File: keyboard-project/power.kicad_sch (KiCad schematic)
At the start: 0 parts

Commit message: working on power
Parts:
- added J1: Conn_01x02, symbol Connector_Generic:Conn_01x02
- added U1: MCP1826S, symbol Regulator_Linear:MCP1826S
- added U2: MCP73871, Package_DFN_QFN:QFN-20-1EP_4x4mm_P0.5mm_EP2.5x2.5mm, symbol Battery_Management:MCP73871
- added U3: XC6206PxxxMR, Package_TO_SOT_SMD:SOT-23-3, symbol Regulator_Linear:XC6206PxxxMR
- added U4: AP7331-28WG-7, AP7331-28WG-7:SOT95P285X145-5N, symbol AP7331-28WG-7:AP7331-28WG-7
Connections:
- new net: U2.1 (OUT), U2.20 (OUT)
- new net: U2.10 (V_{SS}), U2.11 (V_{SS}), U2.21 (V_{SS})
- new net: U2.14 (V_{BAT}), U2.15 (V_{BAT})
- new net: U2.18 (IN), U2.19 (IN)
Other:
- note added: "Battery Charge Controller"
- note added: "Battery Connector"
- note added: "LDO Regulator"
- note added: "Low ESR Voltage Regulator"
- note added: "Regulator"

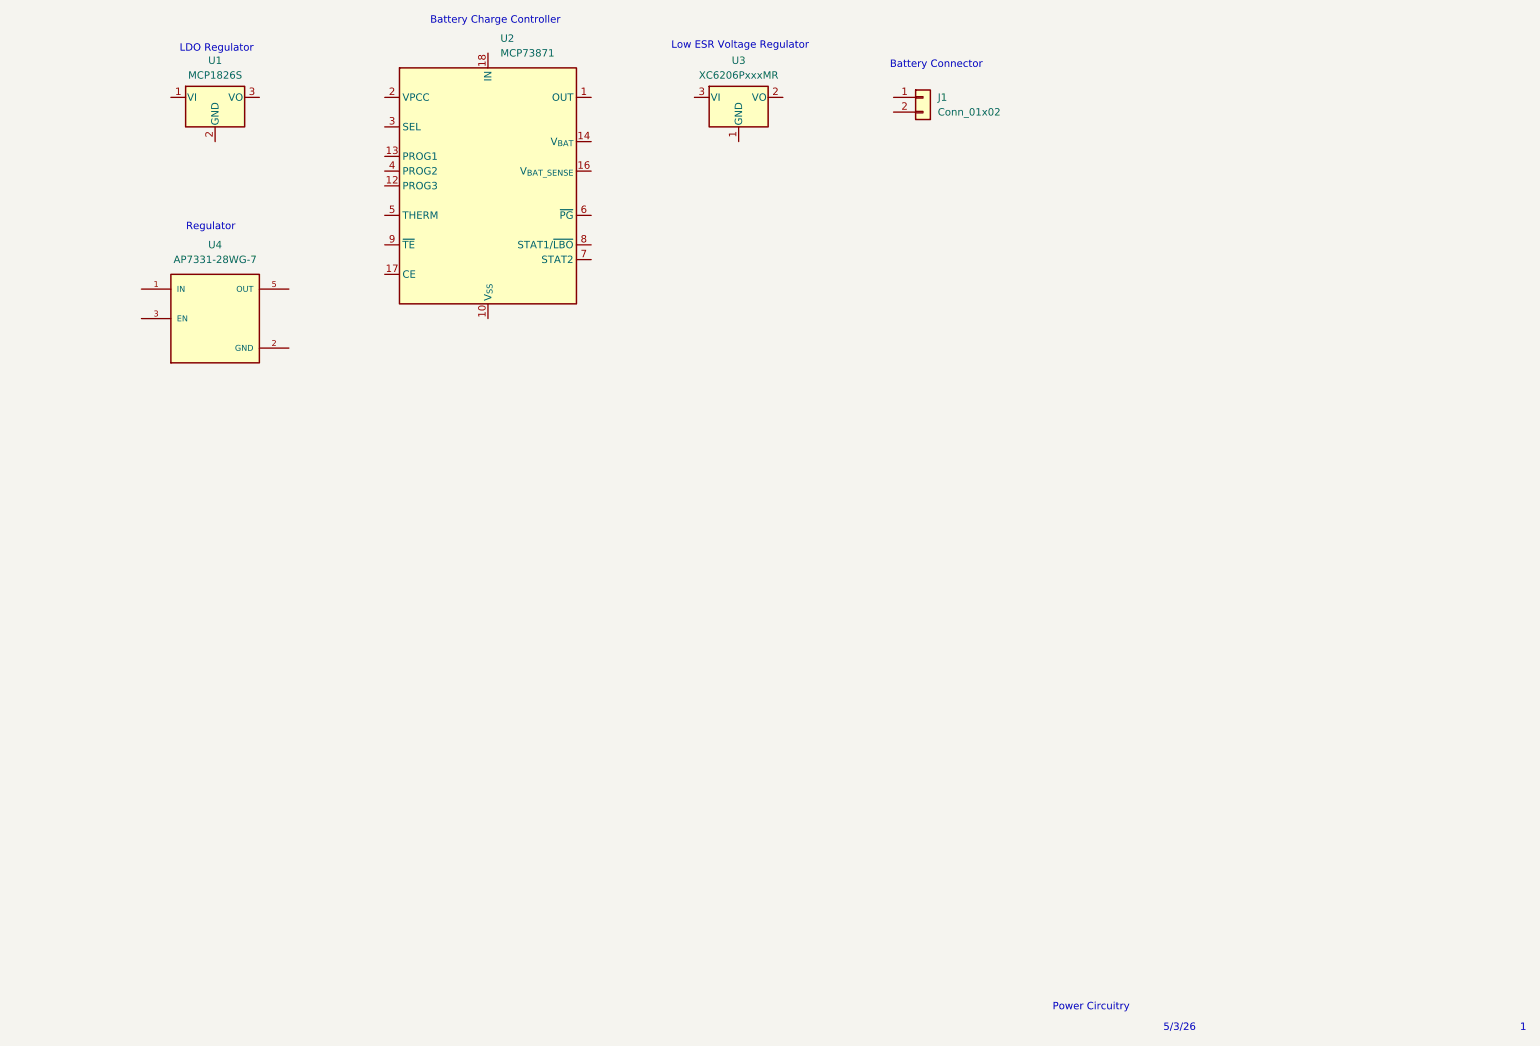
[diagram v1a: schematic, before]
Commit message: power circuitry manufacturer suggested schematics and kicad footprint folder
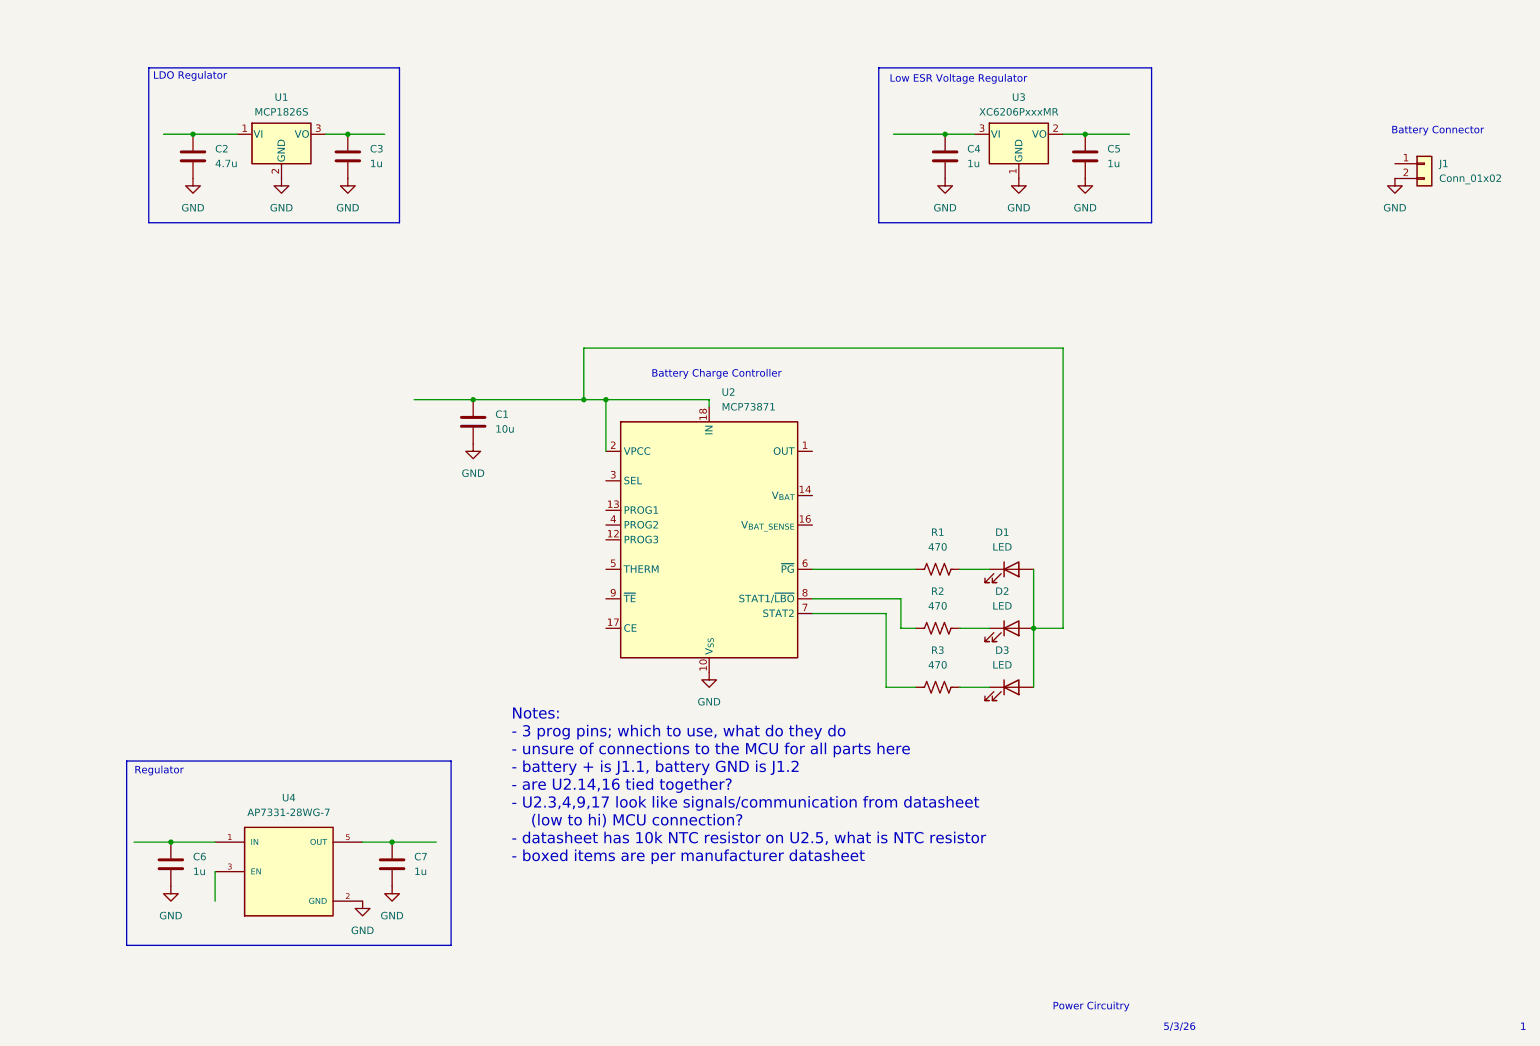
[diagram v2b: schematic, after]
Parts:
- added C1: 10u, symbol Device:C
- added C2: 4.7u, symbol Device:C
- added C3, C4, C5, C6, C7: 1u, symbol Device:C
- added D1, D2, D3: LED, symbol Device:LED
- added R1, R2, R3: 470, symbol Device:R_US
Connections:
- net GND: now reaches U2.10 (V_{SS}), U2.11 (V_{SS}), U2.21 (V_{SS})
- net GND: now also J1.2 (Pin_2), U1.2 (GND), U3.1 (GND), U4.2 (GND), C1.2, C2.2, C3.2, C4.2, C5.2, C6.2, C7.2
- net at U2.18 (IN), U2.19 (IN): now also U2.2 (VPCC), C1.1, D1.2 (A), D2.2 (A), D3.2 (A)
- net at U2.6 (~{PG}): now also R1.1
- net at U2.7 (STAT2): now also R3.1
- net at U2.8 (STAT1/~{LBO}): now also R2.1
- net at U1.1 (VI): now also C2.1
- net at U1.3 (VO): now also C3.1
- net at U4.1 (IN): now also C6.1
- net at U4.5 (OUT): now also C7.1
- net at U3.2 (VO): now also C5.1
- net at U3.3 (VI): now also C4.1
- new net: D1.1 (K), R1.2
- new net: D2.1 (K), R2.2
- new net: D3.1 (K), R3.2
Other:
- note added: "Notes: - 3 prog pins; which to use, what do they do - unsure of connections to the MCU for all parts here - battery + is J1.1, battery GND is J1.2 - are U2.14,16 tied together? - U2.3,4,9,17 look like signals/communication from datasheet (low to hi) MCU connection? - datasheet has 10k NTC resistor on U2.5, what is NTC resistor - boxed items are per manufacturer datasheet"
- moved on the sheet: J1, U1, U2, U3, U4

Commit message: ble update
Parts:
- removed D1: LED, symbol Device:LED
- added C8: 4.7u, symbol Device:C
- added R4: 2k, symbol Device:R_US
- added R5: 20k, symbol Device:R_US
- added R7, R8: R_US, symbol Device:R_US
- added TH1: 10k, symbol Device:Thermistor_US
- D2: value LED -> LED - R
- D3: value LED -> LED - G
- R1: value 470 -> 10k
- R2: value 470 -> 270
- R3: value 470 -> 560
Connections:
- net GND: now also U2.3 (SEL), U2.9 (~{TE}), C8.2, R4.1, R5.2, R8.2, TH1.2
- net at R1.2: now also D3.2 (A)
- net +5V: now reaches C1.1, U2.18 (IN), U2.19 (IN), U2.2 (VPCC)
- net +5V: no longer D2.2 (A), D3.2 (A)
- net CHARGER OUT / REGULATOR IN: now reaches U2.1 (OUT), U2.20 (OUT)
- net CHARGER OUT / REGULATOR IN: now also C2.1, C4.1, C6.1, U1.1 (VI), U3.3 (VI), U4.1 (IN)
- net at U2.12 (PROG3): now also R5.1
- net at U2.13 (PROG1): now also R4.2
- net BAT +: now reaches U2.14 (V_{BAT}), U2.15 (V_{BAT})
- net BAT +: now also J1.1 (Pin_1), U2.16 (V_{BAT_SENSE}), C8.1, R7.1
- net MCP73871 CE: now reaches U2.17 (CE)
- net MCP73871 PROG2: now reaches U2.4 (PROG2)
- net at U2.5 (THERM): now also TH1.1
- net MCP73871 STAT2: now reaches R3.1, U2.7 (STAT2)
- net MCP73871 STAT1: now reaches R2.1, U2.8 (STAT1/~{LBO})
- net +3.3V: now reaches C3.1, U1.3 (VO)
- net +3.3V: now also D2.2 (A)
- net +2: now reaches C7.1, U4.5 (OUT)
- net +3.3VA: now reaches C5.1, U3.2 (VO)
- new net BAT ADC: R7.2, R8.1
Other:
- note added: "battery charge indicator"
- note added: "charge status"
- note added: "low battery"
- note removed: "Notes: - 3 prog pins; which to use, what do they do - unsure of connections to the MCU for all parts here - battery + is J1.1, battery GND is J1.2 - are U2.14,16 tied together? - U2.3,4,9,17 look like signals/communication from datasheet (low to hi) MCU connection? - datasheet has 10k NTC resistor on U2.5, what is NTC resistor - boxed items are per manufacturer datasheet"
- moved on the sheet: C1, C2, C3, C6, C7, D2, D3, J1, R1, R2, R3, U1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

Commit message: encoders, trackball, and display circuits
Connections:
- net CHARGER OUT / REGULATOR IN renamed VS
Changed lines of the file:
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@@
+	)
+	(symbol
+		(lib_id "power:VS")
+		(at 163.83 78.74 0)
+		(unit 1)
+		(body_style 1)
+		(exclude_from_sim no)
+		(in_bom yes)
+		(on_board yes)
+		(in_pos_files yes)
+		(dnp no)
+		(fields_autoplaced yes)
+		(property "Reference" "#PWR099"
+			(at 163.83 82.55 0)
+			(hide yes)
+			(show_name no)
+			(do_not_autoplace no)
+			(effects
+				(font
+					(size 1.27 1.27)
+				)
+			)
+		)
+		(property "Value" "VS"
+			(at 163.83 73.66 0)
+			(show_name no)
+			(do_not_autoplace no)
+			(effects
+				(font
+					(size 1.27 1.27)
+				)
+			)
+		)
+		(property "Footprint" ""
+			(at 163.83 78.74 0)
+			(hide yes)
+			(show_name no)
+			(do_not_autoplace no)
+			(effects
+				(font
+					(size 1.27 1.27)
+				)
+			)
+		)
+		(property "Datasheet" ""
+			(at 163.83 78.74 0)
+			(hide yes)
+			(show_name no)
+			(do_not_autoplace no)
+			(effects
+				(font
+					(size 1.27 1.27)
+				)
+			)
+		)
+		(property "Description" "Power symbol creates a global label with name \"VS\""
+			(at 163.83 78.74 0)
+			(hide yes)
+			(show_name no)
+			(do_not_autoplace no)
+			(effects
+				(font
+					(size 1.27 1.27)
+				)
+			)
+		)
+		(pin "1"
+		)
+		(instances
+			(project "keyboard-project"
+				(path "/20839dd3-8f37-4bf9-a231-e8a616316450/e3c46f0a-4838-4d4b-8e21-c6e226861334"
+					(reference "#PWR099")
+					(unit 1)
+				)
+			)
+		)
 	)
 	(symbol

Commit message: res and cap footprints
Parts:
- C1, C2, C3, C4, C5, C6, C7, C8: footprint (none) -> Capacitor_SMD:C_1206_3216Metric_Pad1.33x1.80mm_HandSolder
- R1, R2, R3, R4, R5, R7, R8: footprint (none) -> Resistor_SMD:R_1206_3216Metric_Pad1.30x1.75mm_HandSolder
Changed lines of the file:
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@@
 			)
 		)
-		(property "Footprint" ""
+		(property "Footprint" "Resistor_SMD:R_1206_3216Metric_Pad1.30x1.75mm_HandSolder"
 			(at 242.316 73.914 90)
 			(hide yes)
@@
 			)
 		)
-		(property "Footprint" ""
+		(property "Footprint" "Resistor_SMD:R_1206_3216Metric_Pad1.30x1.75mm_HandSolder"
 			(at 114.554 96.774 90)
 			(hide yes)
@@
 			)
 		)
-		(property "Footprint" ""
+		(property "Footprint" "Capacitor_SMD:C_1206_3216Metric_Pad1.33x1.80mm_HandSolder"
 			(at 59.3852 49.53 0)
 			(hide yes)
@@
 			)
 		)
-		(property "Footprint" ""
+		(property "Footprint" "Resistor_SMD:R_1206_3216Metric_Pad1.30x1.75mm_HandSolder"
 			(at 242.316 61.214 90)
 			(hide yes)
@@
 			)
 		)
-		(property "Footprint" ""
+		(property "Footprint" "Capacitor_SMD:C_1206_3216Metric_Pad1.33x1.80mm_HandSolder"
 			(at 86.0552 49.53 0)
 			(hide yes)
@@
 			)
 		)
-		(property "Footprint" ""
+		(property "Footprint" "Capacitor_SMD:C_1206_3216Metric_Pad1.33x1.80mm_HandSolder"
 			(at 106.3752 86.36 0)
 			(hide yes)
@@
 			)
 		)
-		(property "Footprint" ""
+		(property "Footprint" "Capacitor_SMD:C_1206_3216Metric_Pad1.33x1.80mm_HandSolder"
 			(at 61.9252 167.64 0)
 			(hide yes)
@@
 			)
 		)
-		(property "Footprint" ""
+		(property "Footprint" "Capacitor_SMD:C_1206_3216Metric_Pad1.33x1.80mm_HandSolder"
 			(at 195.2752 46.99 0)
 			(hide yes)
@@
 			)
 		)
-		(property "Footprint" ""
+		(property "Footprint" "Resistor_SMD:R_1206_3216Metric_Pad1.30x1.75mm_HandSolder"
 			(at 185.674 117.094 90)
 			(hide yes)
@@
 			)
 		)
-		(property "Footprint" ""
+		(property "Footprint" "Capacitor_SMD:C_1206_3216Metric_Pad1.33x1.80mm_HandSolder"
 			(at 100.0252 167.64 0)
 			(hide yes)
@@
 			)
 		)
-		(property "Footprint" ""
+		(property "Footprint" "Capacitor_SMD:C_1206_3216Metric_Pad1.33x1.80mm_HandSolder"
 			(at 192.7352 90.17 0)
 			(hide yes)
@@
 			)
 		)
-		(property "Footprint" ""
+		(property "Footprint" "Capacitor_SMD:C_1206_3216Metric_Pad1.33x1.80mm_HandSolder"
 			(at 171.1452 46.99 0)
 			(hide yes)
@@
 			)
 		)
-		(property "Footprint" ""
+		(property "Footprint" "Resistor_SMD:R_1206_3216Metric_Pad1.30x1.75mm_HandSolder"
 			(at 190.754 106.934 90)
 			(hide yes)
@@
 			)
 		)
-		(property "Footprint" ""
+		(property "Footprint" "Resistor_SMD:R_1206_3216Metric_Pad1.30x1.75mm_HandSolder"
 			(at 84.836 103.886 90)
 			(hide yes)
@@
 			)
 		)
-		(property "Footprint" ""
+		(property "Footprint" "Resistor_SMD:R_1206_3216Metric_Pad1.30x1.75mm_HandSolder"
 			(at 185.674 127.254 90)
 			(hide yes)

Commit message: more footprints
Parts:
- J1: footprint (none) -> Connector_JST:JST_EH_B2B-EH-A_1x02_P2.50mm_Vertical
- U1: footprint (none) -> MCP1826S-3302E_DB:SOT230P700X180-4N
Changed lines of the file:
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@@
 			)
 		)
-		(property "Footprint" ""
+		(property "Footprint" "MCP1826S-3302E_DB:SOT230P700X180-4N"
 			(at 71.12 38.1 0)
 			(hide yes)
@@
 			)
 		)
-		(property "Footprint" ""
+		(property "Footprint" "Connector_JST:JST_EH_B2B-EH-A_1x02_P2.50mm_Vertical"
 			(at 246.38 36.83 0)
 			(hide yes)

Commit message: all footprints in now
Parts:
- D2, D3: footprint (none) -> LED_SMD:LED_1206_3216Metric
- TH1: footprint (none) -> Resistor_SMD:R_01005_0402Metric
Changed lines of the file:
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@@
 			)
 		)
-		(property "Footprint" ""
+		(property "Footprint" "Resistor_SMD:R_01005_0402Metric"
 			(at 107.95 111.76 0)
 			(hide yes)
@@
 			)
 		)
-		(property "Footprint" ""
+		(property "Footprint" "LED_SMD:LED_1206_3216Metric"
 			(at 198.12 118.11 0)
 			(hide yes)
@@
 			)
 		)
-		(property "Footprint" ""
+		(property "Footprint" "LED_SMD:LED_1206_3216Metric"
 			(at 198.12 128.27 0)
 			(hide yes)

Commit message: working on pcb layout, power
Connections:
- net +3.3V: now also D3.2 (A), R1.2, U4.3 (EN)
